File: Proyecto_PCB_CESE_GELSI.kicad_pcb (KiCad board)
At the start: 2 copper layers, 86.4 x 61 mm, 23 parts, among them IC1 SC2272L4, IC2 ASM1117-33, IC3 SN74LVC1G125DCKR, IC4 H5V3G

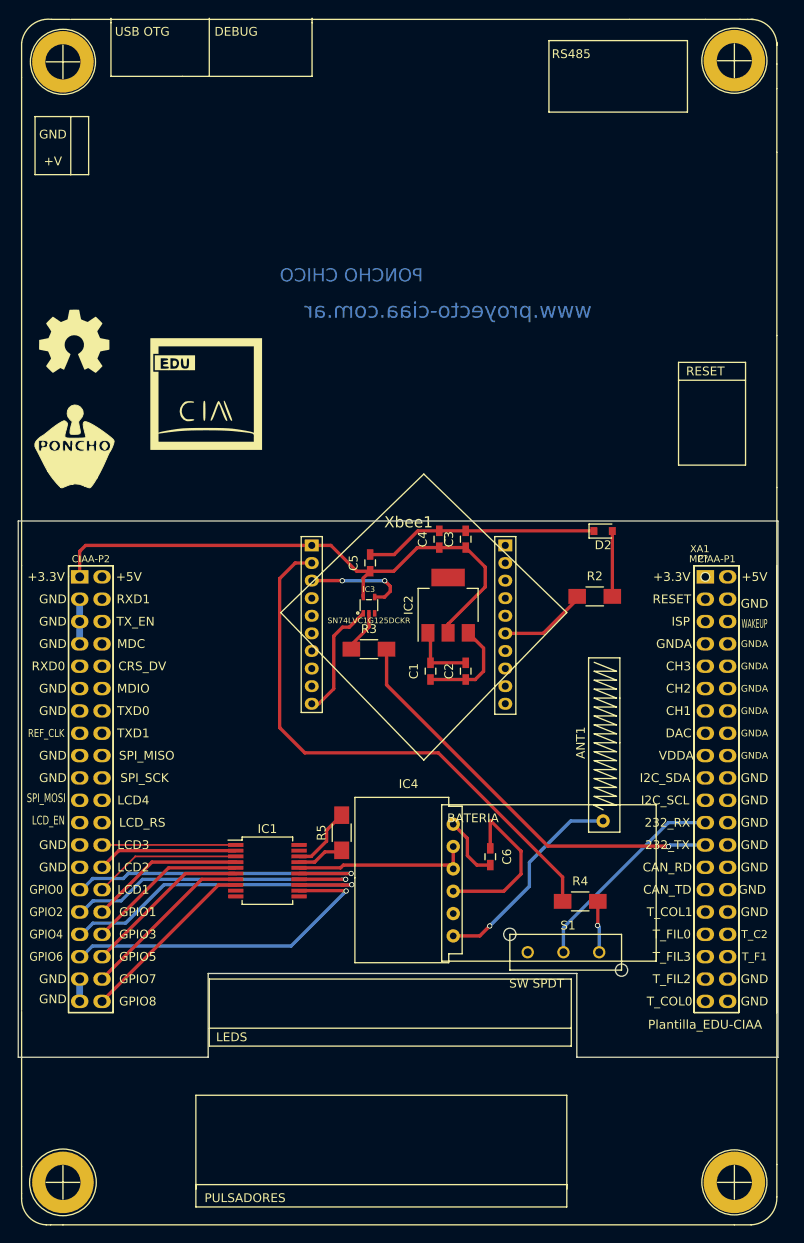
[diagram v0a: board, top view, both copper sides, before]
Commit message: Update en proyecto
Se resolvieron algunos problemas referidos al PCB, a fin de corregir los errores marcados durante la primer entrega. Por problemas con el IDE KICAD, se dejaron algunos para la tercer entrega.
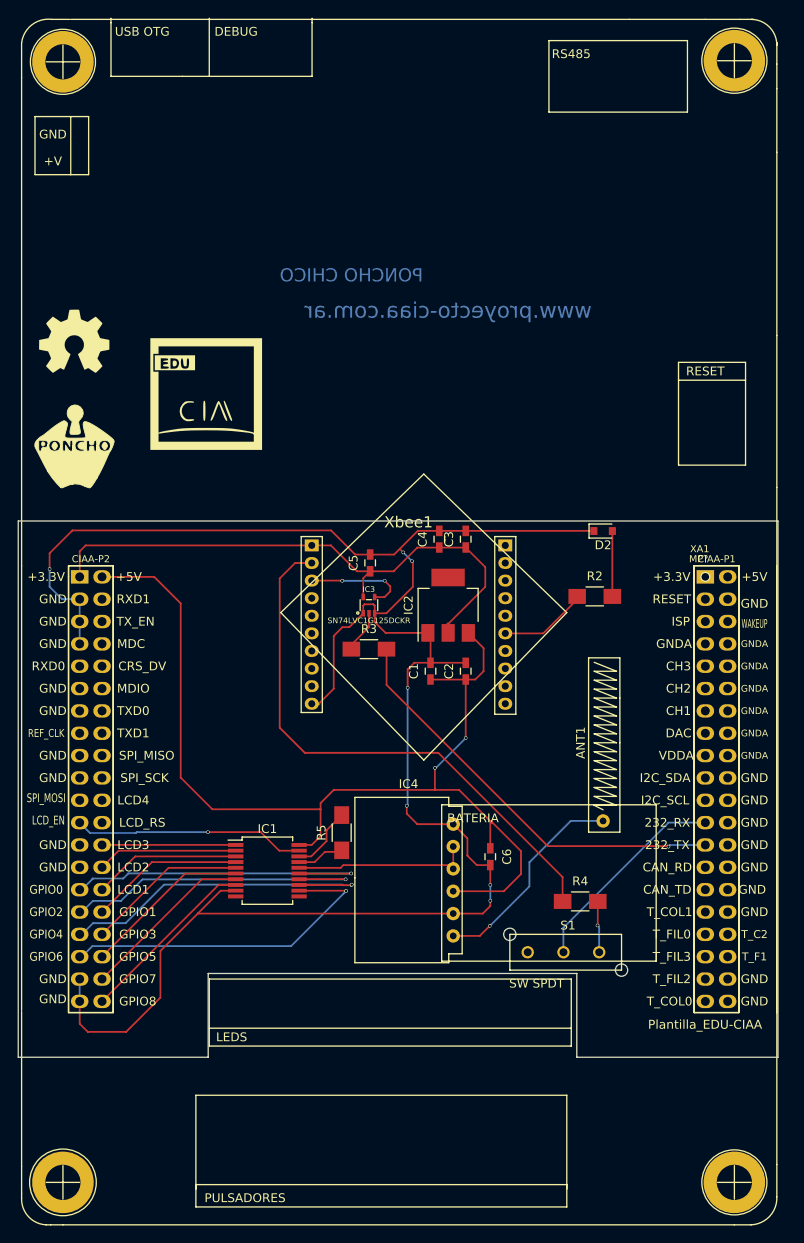
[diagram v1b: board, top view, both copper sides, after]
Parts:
- R4: value 22R -> 22
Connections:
- net /RX renamed Net-(S1-Pad2)
- net /TX renamed Net-(R3-Pad2)
- net /VT renamed Net-(IC1-Pad19)
- XA1 pad 41: +3.3V -> Net-(XA1-Pad41)
- XA1 pad 42: Net-(XA1-Pad42) -> +5V
- XA1 pad 43: Net-(XA1-Pad43) -> GND
- XA1 pad 79: Net-(XA1-Pad79) -> GND
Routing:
- net GND: track 55.0 -> 219.1 mm, vias 0 -> 7
- net +5V: track 30.7 -> 120.7 mm, vias 0 -> 2
- net Net-(IC1-Pad19): track 0.00 -> 26.3 mm, vias 0 -> 1
- net Net-(XA1-Pad41): track 0.00 -> 2.90 mm
- net +3.3V: track 65.0 -> 62.1 mm
- net Net-(XA1-Pad43): track 2.54 -> 0.00 mm
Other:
- net class Default: clearance 0.508 -> 0.15; trace_width 0.381 -> 0.2; via_dia 0.6 -> 0.4; via_drill 0.4 -> 0.3
- net class ic1_margen: clearance 0.17 -> 0.15; trace_width 0.381 -> 0.2
- rule trace_clearance: 0.508 -> 0.15
- board text added: "Grilla: 0,25 mm Pista: 0,20 mm Vía: 0,40 mm Agujero: 0,40 mm"
- board text removed: "Editar el rótulo"
- board text removed: "Editar el stackup para reflejar cantidad de capas, si se han realizado cálculos de impedancia o si es relevante para el funcionamiento."

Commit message: Correciones totales al esquemático, pcb y organización parcial en visor 3D
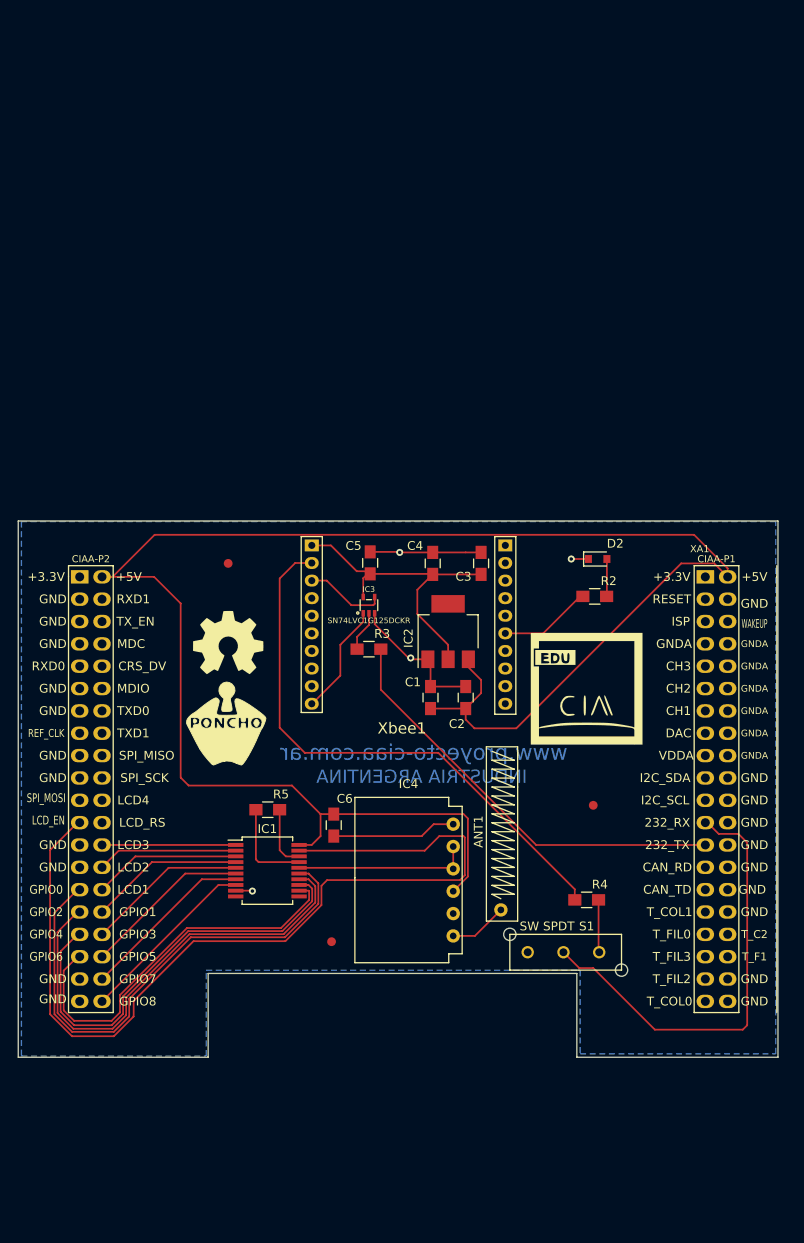
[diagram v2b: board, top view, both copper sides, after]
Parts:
- removed MP?: Plantilla_EDU-CIAA, Poncho_Esqueleto:Plantilla_EDU-CIAA
- added F1: FIDUCIAL, projectHuellas:Fiducial_1mm, F.Cu at (88.0, 79.8)
- added F2: FIDUCIAL, projectHuellas:Fiducial_1mm, F.Cu at (99.8, 122.8)
- added F3: FIDUCIAL, projectHuellas:Fiducial_1mm, F.Cu at (129.5, 107.2)
- C1, C2, C3, C4, C5, C6: footprint projectHuellas:C_0603_HandSoldering -> projectHuellas:C_0805_HandSoldering
- R2, R3, R4, R5: footprint projectHuellas:R_1206_HandSoldering -> projectHuellas:R_0805_HandSoldering
- moved G*** 54.7 mm to (128.8, 94.0)
- moved G101 38.5 mm to (88.0, 88.8)
- moved G*** 35.9 mm to (87.8, 98.0)
- moved C6 18.2 mm to (100.0, 109.5)
- moved ANT1 15.4 mm to (119.0, 110.2)
- moved R5 8.80 mm to (92.5, 107.8), turned to 0 degrees
- moved C3 3.26 mm to (116.8, 79.8)
- moved D2 3.24 mm to (130.0, 79.2)
- moved C1 3.00 mm to (111.0, 95.0)
- moved C2 3.00 mm to (115.0, 95.0)
- moved IC2 3.00 mm to (113.0, 87.5)
- moved C4 2.85 mm to (111.2, 79.8)
- moved R4 0.75 mm to (128.8, 118.0)
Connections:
- C1 pad 1: +5V -> Net-(C1-Pad1)
- C1 pad 2: GND -> Net-(C1-Pad2)
- C2 pad 1: +5V -> Net-(C2-Pad1)
- C2 pad 2: GND -> Net-(C2-Pad2)
- C3 pad 1: +3.3V -> Net-(C3-Pad1)
- C3 pad 2: GND -> Net-(C3-Pad2)
- C4 pad 1: +3.3V -> Net-(C4-Pad1)
- C4 pad 2: GND -> Net-(C4-Pad2)
- C5 pad 1: +3.3V -> Net-(C5-Pad1)
- C5 pad 2: GND -> Net-(C5-Pad2)
- C6 pad 1: +5V -> Net-(C6-Pad1)
- C6 pad 2: GND -> Net-(C6-Pad2)
- XA1 pad 2: Net-(XA1-Pad2) -> +5V
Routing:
- net GND: track 219.1 -> 59.9 mm, vias 7 -> 4
- net +5V: track 120.7 -> 205.4 mm, vias 2 -> 0
- net Net-(IC1-Pad19): track 26.3 -> 105.3 mm, vias 1 -> 0
- net Net-(S1-Pad2): track 23.9 -> 51.2 mm
- net +3.3V: track 62.1 -> 35.6 mm
- net Net-(IC1-Pad15): track 37.6 -> 58.7 mm, vias 1 -> 0
- net Net-(ANT1-Pad1): track 24.1 -> 6.66 mm, vias 1 -> 0
- net Net-(IC1-Pad14): track 37.1 -> 54.1 mm, vias 1 -> 0
- net Net-(IC1-Pad13): track 39.4 -> 49.4 mm, vias 1 -> 0
- net Net-(IC1-Pad12): track 38.8 -> 44.6 mm, vias 1 -> 0
- net Net-(IC1-Pad17): track 5.40 -> 10.7 mm
- net Net-(D2-Pad2): track 7.43 -> 4.27 mm
- net Net-(XA1-Pad41): track 2.90 -> 0.00 mm
- net Net-(IC3-Pad4): track 11.8 -> 9.14 mm, vias 2 -> 0
- net Net-(XA1-Pad45): track 2.54 -> 0.00 mm
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- added copper zone on B.Cu, net GND
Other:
- board text added: "Grilla: 0,25 mm Pista: 0,20 mm Vía: 0,80 mm Agujero: 0,40 mm"
- board text added: "INDUSTRIA ARGENTINA"
- board text removed: "Borrar (Footprint MP1) la Plantilla-EDU-CIAA al finalizar el posicionamiento y definido el borde de PCB."
- board text removed: "Grilla: 0,25 mm Pista: 0,20 mm Vía: 0,40 mm Agujero: 0,40 mm"
- board text removed: "PONCHO CHICO"
- board text removed: "PONCHO CHICO http://www.proyecto-ciaa.com.ar/"
- board text removed: "Para un diseño nuevo luego de modificar el esquemático: 1)Seleccionar el bloque del PCB y cotas. (click-drag-release). 2)Opción de borrar bloque (Botón derecho). 3)Marcar todo menos locked footprints (MP1 y XA1) 4) Aceptar. 5) Volver a cargar el netlist."
- board text removed: "Se sugiere colocar código de Poncho en cobre, serigrafía y rótulo."

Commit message: Update final a producción.
Subida final de archivos para sustentar las cosas a corregir marcadas por el profesor. Faltantes no conseguidos en visión 3D.
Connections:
- C1 pad 1: Net-(C1-Pad1) -> +5V
- C1 pad 2: Net-(C1-Pad2) -> GND
- C2 pad 1: Net-(C2-Pad1) -> +5V
- C2 pad 2: Net-(C2-Pad2) -> GND
- C3 pad 1: Net-(C3-Pad1) -> +3.3V
- C3 pad 2: Net-(C3-Pad2) -> GND
- C4 pad 1: Net-(C4-Pad1) -> +3.3V
- C4 pad 2: Net-(C4-Pad2) -> GND
- C5 pad 1: Net-(C5-Pad1) -> +3.3V
- C5 pad 2: Net-(C5-Pad2) -> GND
- C6 pad 1: Net-(C6-Pad1) -> +5V
- C6 pad 2: Net-(C6-Pad2) -> GND
